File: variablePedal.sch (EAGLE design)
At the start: 0 parts

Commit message: Parts selected and placed (values TBD)
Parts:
- added C1, C2: (no value), rcl:C-USC1206
- added IC1: OPA340U, burr-brown:OPA340U
- added J2, J3: AUDIO_JACK_TRS_0.25"_PTH_RA, SparkFun-Connectors:AUDIO_JACK_TRS_0.25"_PTH_RA
- added J4: 5.5x2.1mm Barrel, SparkFun-Connectors:POWER_JACKSMD
- added Q1: MPSA56, transistor-pnp:MPSA56
- added R1, R2, R6: (no value), rcl:POTENTIOMETER_PT-10
- added R3, R4, R5: (no value), rcl:R-US_R0805
- added TM1, TM2: (no value), adafruit:TRIMPOTTC33X
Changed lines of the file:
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@@
 <layer number="112" name="tSilk" color="7" fill="1" visible="no" active="yes"/>
 <layer number="113" name="ReferenceLS" color="7" fill="1" visible="no" active="no"/>
+<layer number="114" name="Badge_Outline" color="7" fill="1" visible="yes" active="yes"/>
+<layer number="115" name="ReferenceISLANDS" color="7" fill="1" visible="yes" active="yes"/>
 <layer number="116" name="Patch_BOT" color="9" fill="4" visible="no" active="yes"/>
 <layer number="118" name="Rect_Pads" color="7" fill="1" visible="no" active="no"/>
@@
 </classes>
 <parts>
+<part name="TM1" library="adafruit" library_urn="urn:adsk.eagle:library:420" deviceset="TRIMPOT" device="TC33X" package3d_urn="urn:adsk.eagle:package:6240639/1"/>
+<part name="TM2" library="adafruit" library_urn="urn:adsk.eagle:library:420" deviceset="TRIMPOT" device="TC33X" package3d_urn="urn:adsk.eagle:package:6240639/1"/>
+<part name="R1" library="rcl" library_urn="urn:adsk.eagle:library:334" deviceset="POTENTIOMETER_" device="PT-10" package3d_urn="urn:adsk.eagle:package:23786/1"/>
+<part name="R2" library="rcl" library_urn="urn:adsk.eagle:library:334" deviceset="POTENTIOMETER_" device="PT-10" package3d_urn="urn:adsk.eagle:package:23786/1"/>
+<part name="P+1" library="supply1" library_urn="urn:adsk.eagle:library:371" deviceset="V+" device=""/>
+<part name="GND1" library="supply1" library_urn="urn:adsk.eagle:library:371" deviceset="GND" device=""/>
+<part name="IC1" library="burr-brown" library_urn="urn:adsk.eagle:library:111" deviceset="OPA340" device="U" package3d_urn="urn:adsk.eagle:package:4924/1"/>
+<part name="C1" library="rcl" library_urn="urn:adsk.eagle:library:334" deviceset="C-US" device="C1206" package3d_urn="urn:adsk.eagle:package:23618/2"/>
+<part name="Q1" library="transistor-pnp" library_urn="urn:adsk.eagle:library:399" deviceset="MPSA56*" device="" package3d_urn="urn:adsk.eagle:package:29223/2"/>
+<part name="C2" library="rcl" library_urn="urn:adsk.eagle:library:334" deviceset="C-US" device="C1206" package3d_urn="urn:adsk.eagle:package:23618/2"/>
+<part name="R3" library="rcl" library_urn="urn:adsk.eagle:library:334" deviceset="R-US_" device="R0805" package3d_urn="urn:adsk.eagle:package:23553/2"/>
+<part name="R4" library="rcl" library_urn="urn:adsk.eagle:library:334" deviceset="R-US_" device="R0805" package3d_urn="urn:adsk.eagle:package:23553/2"/>
+<part name="R5" library="rcl" library_urn="urn:adsk.eagle:library:334" deviceset="R-US_" device="R0805" package3d_urn="urn:adsk.eagle:package:23553/2"/>
+<part name="R6" library="rcl" library_urn="urn:adsk.eagle:library:334" deviceset="POTENTIOMETER_" device="PT-10" package3d_urn="urn:adsk.eagle:package:23786/1"/>
+<part name="J2" library="SparkFun-Connectors" library_urn="urn:adsk.eagle:library:513" deviceset="AUDIO_JACK_TRS_0.25&quot;_PTH_RA" device="" package3d_urn="urn:adsk.eagle:package:38295/1"/>
+<part name="J3" library="SparkFun-Connectors" library_urn="urn:adsk.eagle:library:513" deviceset="AUDIO_JACK_TRS_0.25&quot;_PTH_RA" device="" package3d_urn="urn:adsk.eagle:package:38295/1"/>
+<part name="J4" library="SparkFun-Connectors" library_urn="urn:adsk.eagle:library:513" deviceset="POWER_JACK" device="SMD" package3d_urn="urn:adsk.eagle:package:38221/1" value="5.5x2.1mm Barrel"/>
 </parts>
 <sheets>
@@
 </plain>
 <instances>
+<instance part="TM1" gate="G$1" x="63.5" y="81.28" smashed="yes">
+<attribute name="NAME" x="57.531" y="77.47" size="1.778" layer="95" rot="R90"/>
+<attribute name="VALUE" x="59.69" y="77.47" size="1.778" layer="96" rot="R90"/>
+</instance>
+<instance part="TM2" gate="G$1" x="86.36" y="50.8" smashed="yes">
+<attribute name="NAME" x="80.391" y="46.99" size="1.778" layer="95" rot="R90"/>
+<attribute name="VALUE" x="82.55" y="46.99" size="1.778" layer="96" rot="R90"/>
+</instance>
+<instance part="R1" gate="1" x="86.36" y="81.28" smashed="yes" rot="R90">
+<attribute name="NAME" x="91.44" y="83.82" size="1.778" layer="95" rot="R90"/>
+<attribute name="VALUE" x="93.98" y="83.82" size="1.778" layer="96" rot="R90"/>
+</instance>
+<instance part="R2" gate="1" x="63.5" y="50.8" smashed="yes" rot="R90">
+<attribute name="NAME" x="68.58" y="53.34" size="1.778" layer="95" rot="R90"/>
+<attribute name="VALUE" x="71.12" y="53.34" size="1.778" layer="96" rot="R90"/>
+</instance>
+<instance part="P+1" gate="1" x="170.18" y="30.48" smashed="yes" rot="R180">
+<attribute name="VALUE" x="175.26" y="35.56" size="1.778" layer="96" rot="R270"/>
+</instance>
+<instance part="GND1" gate="1" x="170.18" y="93.98" smashed="yes" rot="R180">
+<attribute name="VALUE" x="172.72" y="96.52" size="1.778" layer="96" rot="R180"/>
+</instance>
+<instance part="IC1" gate="G$1" x="116.84" y="60.96" smashed="yes">
+<attribute name="NAME" x="119.38" y="66.675" size="1.778" layer="95"/>
+<attribute name="VALUE" x="119.38" y="55.88" size="1.778" layer="96"/>
+</instance>
+<instance part="C1" gate="G$1" x="33.02" y="66.04" smashed="yes" rot="R90">
+<attribute name="NAME" x="32.385" y="67.056" size="1.778" layer="95" rot="R90"/>
+<attribute name="VALUE" x="37.211" y="67.056" size="1.778" layer="96" rot="R90"/>
+</instance>
+<instance part="Q1" gate="G$1" x="83.82" y="66.04" smashed="yes" rot="MR180">
+<attribute name="NAME" x="73.66" y="58.42" size="1.778" layer="95" rot="MR180"/>
+<attribute name="VALUE" x="73.66" y="60.96" size="1.778" layer="96" rot="MR180"/>
+</instance>
+<instance part="C2" gate="G$1" x="93.98" y="71.12" smashed="yes" rot="R90">
+<attribute name="NAME" x="93.345" y="72.136" size="1.778" layer="95" rot="R90"/>
+<attribute name="VALUE" x="98.171" y="72.136" size="1.778" layer="96" rot="R90"/>
+</instance>
+<instance part="R3" gate="G$1" x="106.68" y="71.12" smashed="yes">
+<attribute name="NAME" x="102.87" y="72.6186" size="1.778" layer="95"/>
+<attribute name="VALUE" x="102.87" y="67.818" size="1.778" layer="96"/>
+</instance>
+<instance part="R4" gate="G$1" x="106.68" y="53.34" smashed="yes" rot="R90">
+<attribute name="NAME" x="105.1814" y="49.53" size="1.778" layer="95" rot="R90"/>
+<attribute name="VALUE" x="109.982" y="49.53" size="1.778" layer="96" rot="R90"/>
+</instance>
+<instance part="R5" gate="G$1" x="106.68" y="83.82" smashed="yes" rot="R90">
+<attribute name="NAME" x="105.1814" y="80.01" size="1.778" layer="95" rot="R90"/>
+<attribute name="VALUE" x="109.982" y="80.01" size="1.778" layer="96" rot="R90"/>
+</instance>
+<instance part="R6" gate="1" x="132.08" y="71.12" smashed="yes">
+<attribute name="NAME" x="134.62" y="66.04" size="1.778" layer="95"/>
+<attribute name="VALUE" x="134.62" y="63.5" size="1.778" layer="96"/>
+</instance>
+<instance part="J2" gate="G$1" x="12.7" y="63.5" smashed="yes">
+<attribute name="NAME" x="7.62" y="71.628" size="1.778" layer="95"/>
+<attribute name="VALUE" x="7.62" y="55.88" size="1.778" layer="96"/>
+</instance>
+<instance part="J3" gate="G$1" x="149.86" y="58.42" smashed="yes" rot="MR0">
+<attribute name="NAME" x="154.94" y="66.548" size="1.778" layer="95" rot="MR0"/>
+<attribute name="VALUE" x="154.94" y="48.26" size="1.778" layer="96" rot="MR0"/>
+</instance>
+<instance part="J4" gate="G$1" x="190.5" y="68.58" smashed="yes" rot="MR0">
+<attribute name="VALUE" x="200.66" y="78.74" size="1.778" layer="96" font="vector" rot="MR0"/>
+<attribute name="NAME" x="200.66" y="68.58" size="1.778" layer="95" font="vector" rot="MR0"/>
+</instance>
 </instances>
 <busses>
@@
 </schematic>
 </drawing>
+<compatibility>
+<note version="8.2" severity="warning">
+Since Version 8.2, EAGLE supports online libraries. The ids
+of those online libraries will not be understood (or retained)
+with this version.
+</note>
+<note version="8.3" severity="warning">
+Since Version 8.3, EAGLE supports URNs for individual library
+assets (packages, symbols, and devices). The URNs of those assets
+will not be understood (or retained) with this version.
+</note>
+<note version="8.3" severity="warning">
+Since Version 8.3, EAGLE supports the association of 3D packages
+with devices in libraries, schematics, and board files. Those 3D
+packages will not be understood (or retained) with this version.
+</note>
+<note version="8.4" severity="warning">
+Since Version 8.4, EAGLE supports properties for SPICE simulation.
+Probes in schematics and SPICE mapping objects found in parts and library devices
+will not be understood with this version. Update EAGLE to the latest version
+for full support of SPICE simulation.
+</note>
+</compatibility>
 </eagle>

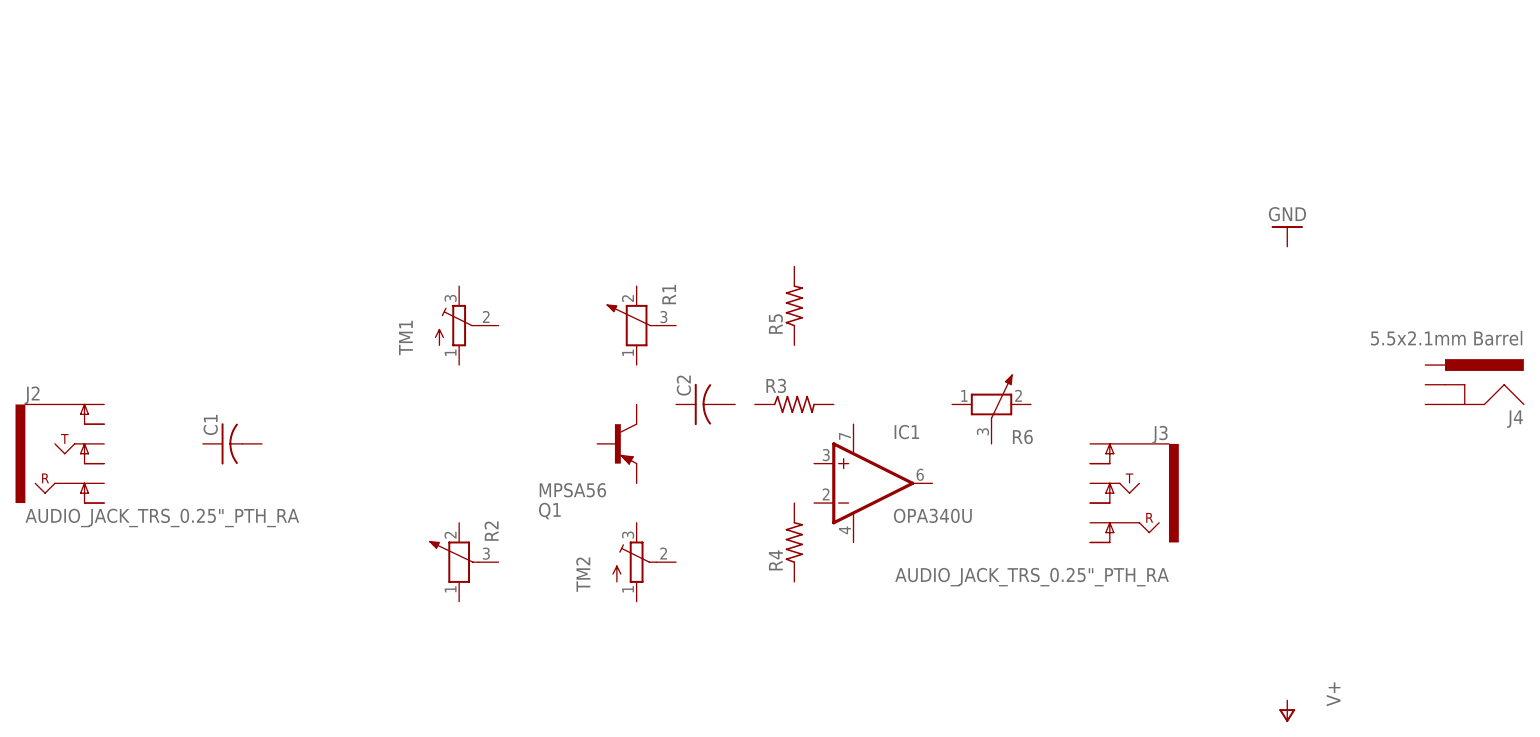
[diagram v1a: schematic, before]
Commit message: Routed nets, ERC indicates no values
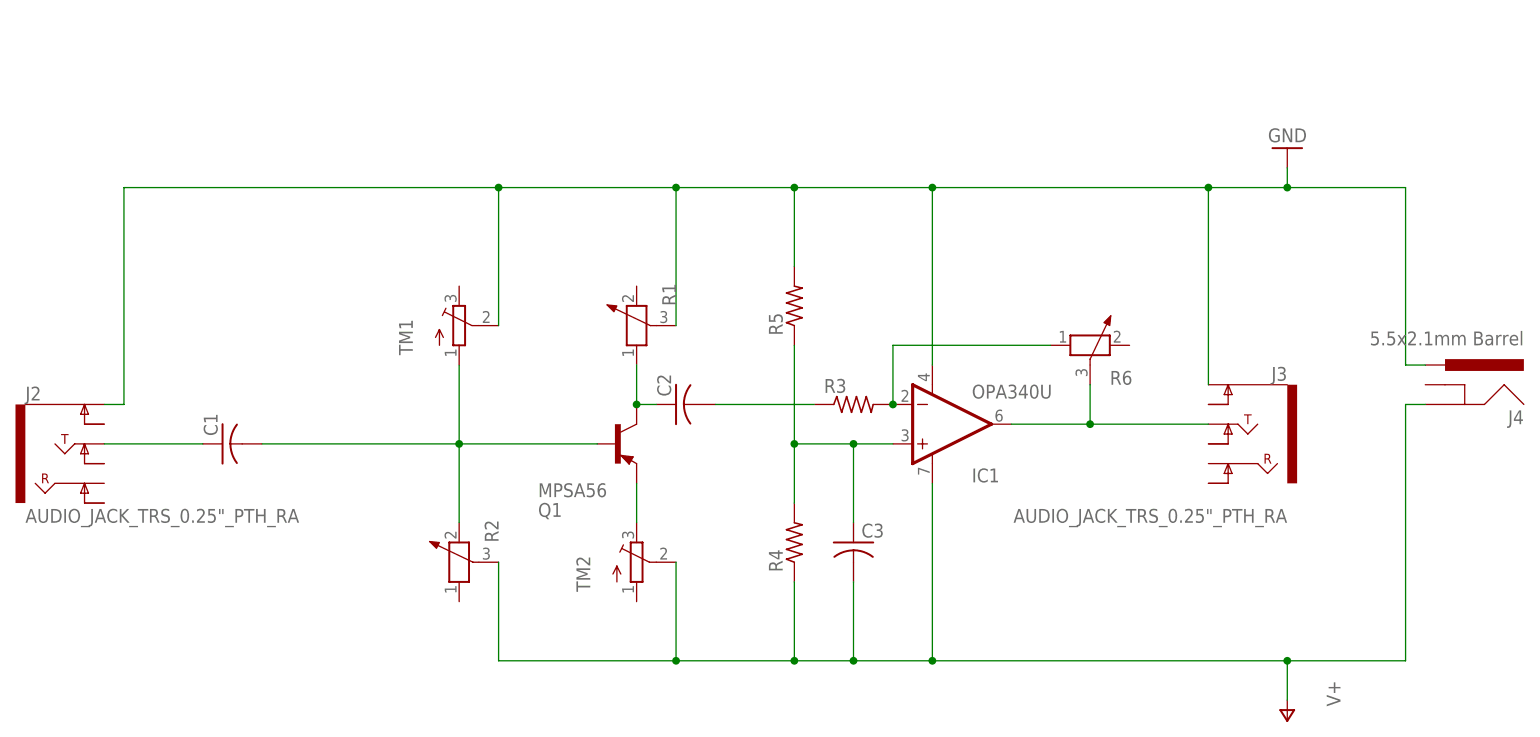
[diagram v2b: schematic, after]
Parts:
- added C3: (no value), rcl:C-USC1206
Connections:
- new net GND: IC1.V-, J2.EARTH, J3.EARTH, J4.PWR, R1.3, R5.2, TM1.S
- new net N$1: C1.2, Q1.B, R2.2, TM1.A
- new net N$11: C1.1, J2.TIP
- new net N$2: C2.1, Q1.C, R1.1
- new net N$3: Q1.E, TM2.E
- new net N$4: C2.2, R3.1
- new net N$5: C3.1, IC1.+IN, R4.2, R5.1
- new net N$6: IC1.-IN, R3.2, R6.1
- new net N$7: IC1.OUT, J3.TIP, R6.3
- new net V+: C3.2, IC1.V+, J4.GND, R2.3, R4.1, TM2.S
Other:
- moved on the sheet: C2, IC1, J3, R3, R6

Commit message: parts placed
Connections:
- net V+: now also J4.GNDBREAK
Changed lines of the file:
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@@
 <wire x1="185.42" y1="38.1" x2="170.18" y2="38.1" width="0.1524" layer="91"/>
 <junction x="170.18" y="38.1"/>
+<pinref part="J4" gate="G$1" pin="GNDBREAK"/>
+<wire x1="187.96" y1="73.66" x2="185.42" y2="73.66" width="0.1524" layer="91"/>
+<wire x1="185.42" y1="73.66" x2="185.42" y2="71.12" width="0.1524" layer="91"/>
+<junction x="185.42" y="71.12"/>
 </segment>
 </net>

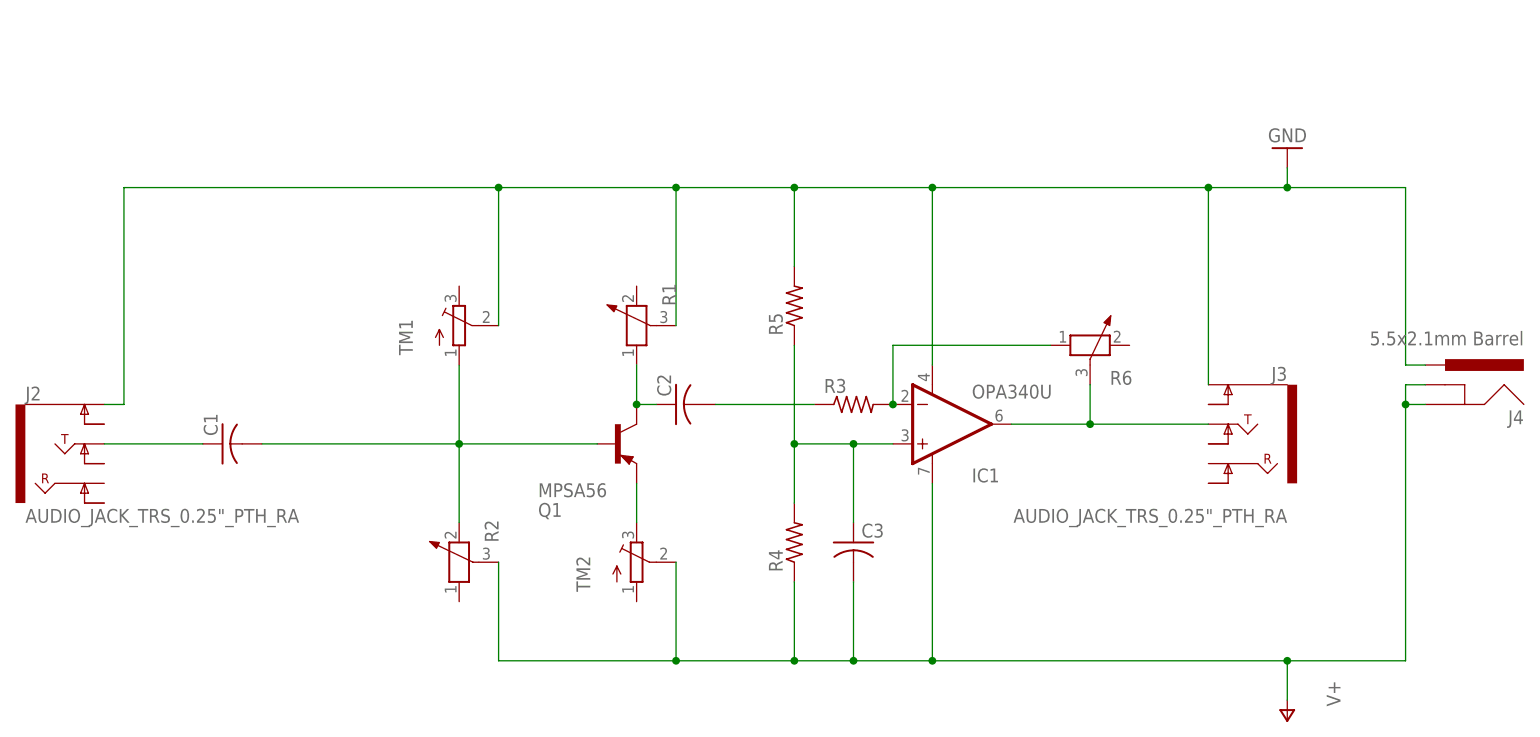
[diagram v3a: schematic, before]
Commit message: Updated schematic with socket, created BOM and Gerbers
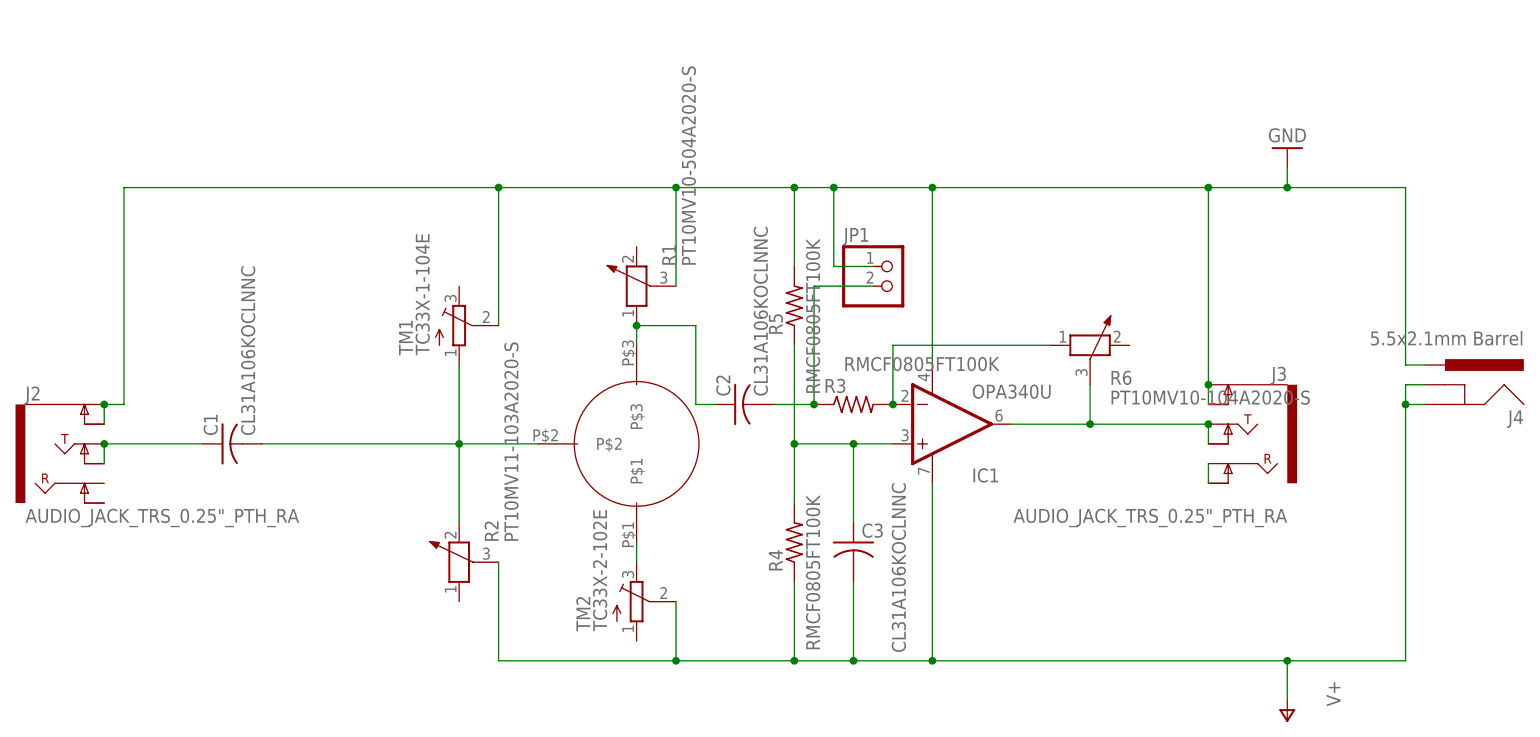
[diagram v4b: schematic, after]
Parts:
- removed Q1: MPSA56, transistor-pnp:MPSA56
- added JP1: (no value), pinhead:PINHD-1X2
- added U$1: 917-43-103-41-005000, FormE:917-43-103-41-005000
- C1, C2, C3: value (none) -> CL31A106KOCLNNC
- R1: value (none) -> PT10MV10-504A2020-S
- R2: value (none) -> PT10MV11-103A2020-S
- R3, R4, R5: value (none) -> RMCF0805FT100K
- R6: value (none) -> PT10MV10-104A2020-S
- TM1: value (none) -> TC33X-1-104E
- TM2: value (none) -> TC33X-2-102E
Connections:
- new net N$8: J3.RING, J3.RING-NORM
- net GND: now also J2.EARTH-NORM, J3.EARTH-NORM, JP1.1
- net N$1: now also U$1.P$2; no longer Q1.B
- net N$11: now also J2.TIP-NORM
- net N$2: now also U$1.P$3; no longer Q1.C
- net N$3: now also U$1.P$1; no longer Q1.E
- net N$4: now also JP1.2
- net N$7: now also J3.TIP-NORM
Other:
- moved on the sheet: C2, R1, TM2
